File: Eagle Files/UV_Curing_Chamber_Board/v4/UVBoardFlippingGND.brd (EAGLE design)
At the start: 143.3 x 88.4 mm, 29 parts, among them IC1 7805T, IC2 L293D, T1 RFP30N06LE, T2 RFP30N06LE

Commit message: Updated V4
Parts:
- C1, C4, C5, C6, C7: device rcl:C075-063X106 -> rcl:C0603
- C2, C3: device rcl:E1,8-4 -> rcl:C1206
- R1, R2, R3, R5: device rcl:0207/10 -> rcl:R0805
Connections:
- net +5V: now also C3.1; no longer C3.+
- net GND: now also C2.2, C3.2; no longer C2.-, C3.-
- net V+: now also C2.1; no longer C2.+
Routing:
- net +3V3: track 117.3 -> 0.00 mm
- net N$11: track 50.8 -> 0.00 mm
- net N$10: track 48.7 -> 0.00 mm
- net N$25: track 48.0 -> 0.00 mm
- net N$24: track 48.0 -> 0.00 mm
- net N$22: track 46.9 -> 0.00 mm
- net GND: track 17.0 -> 0.00 mm
- net N$17: track 10.4 -> 0.00 mm
- removed copper zone on layer 1, net GND
- removed copper zone on layer 16, net GND
- removed copper zone on layer 1, net V+

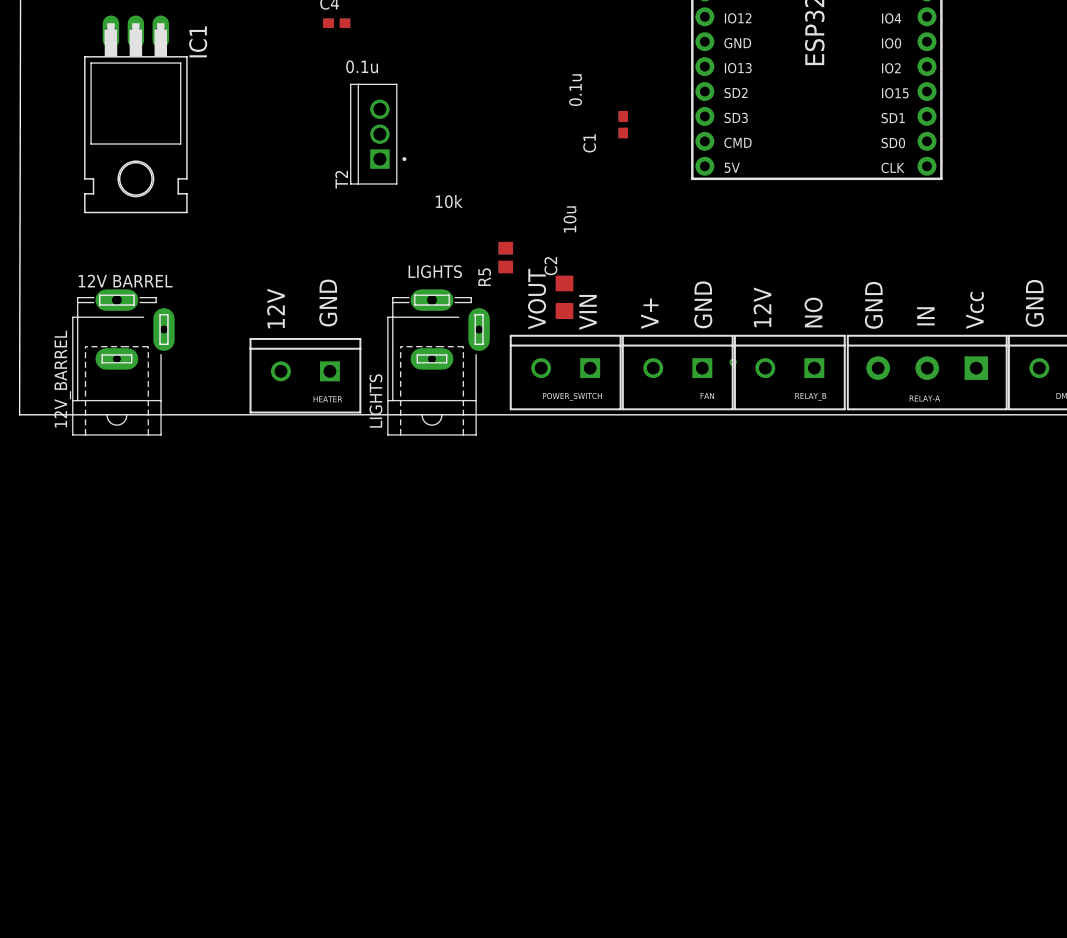
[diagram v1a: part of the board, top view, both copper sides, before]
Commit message: V4 board now has relay circuit on board.
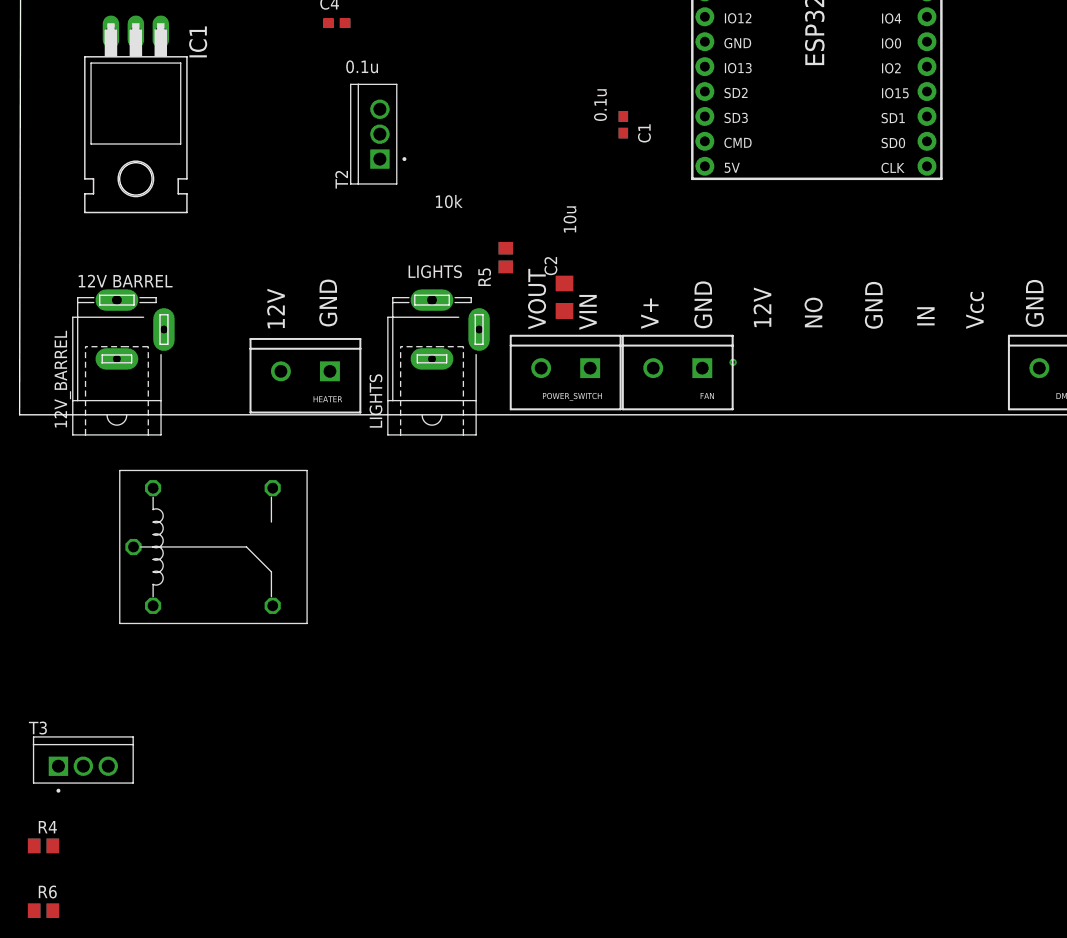
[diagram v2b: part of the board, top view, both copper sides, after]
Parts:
- removed RELAY-A: (no value), SparkFun-Connectors:SCREWTERMINAL-5MM-3
- removed RELAY_B: (no value), SparkFun-Connectors:SCREWTERMINAL-5MM-2
- added R4: 10k, rcl:R0805
- added R6: 220, rcl:R0805
- added T3: RFP30N06LE, RFP30N06LE:TRANS_RFP30N06LE
- added U$2: RELAY, RELAY:RELAY
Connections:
- new net N$31: T3.2, U$2.P$2
- new net N$32: R6.2, U$2.P$1
- net +3V3: no longer DM_SWITCH.1
- net +5V: now also DM_SWITCH.1
- net GND: now also R4.1, T3.3; no longer RELAY-A.3
- net N$16: now also R4.2, T3.1; no longer RELAY-A.2
- net N$28: now also U$2.COM_CPEN; no longer RELAY_B.1
- net N$8: now also R6.1; no longer RELAY-A.1
- net V+: now also U$2.COM; no longer RELAY_B.2

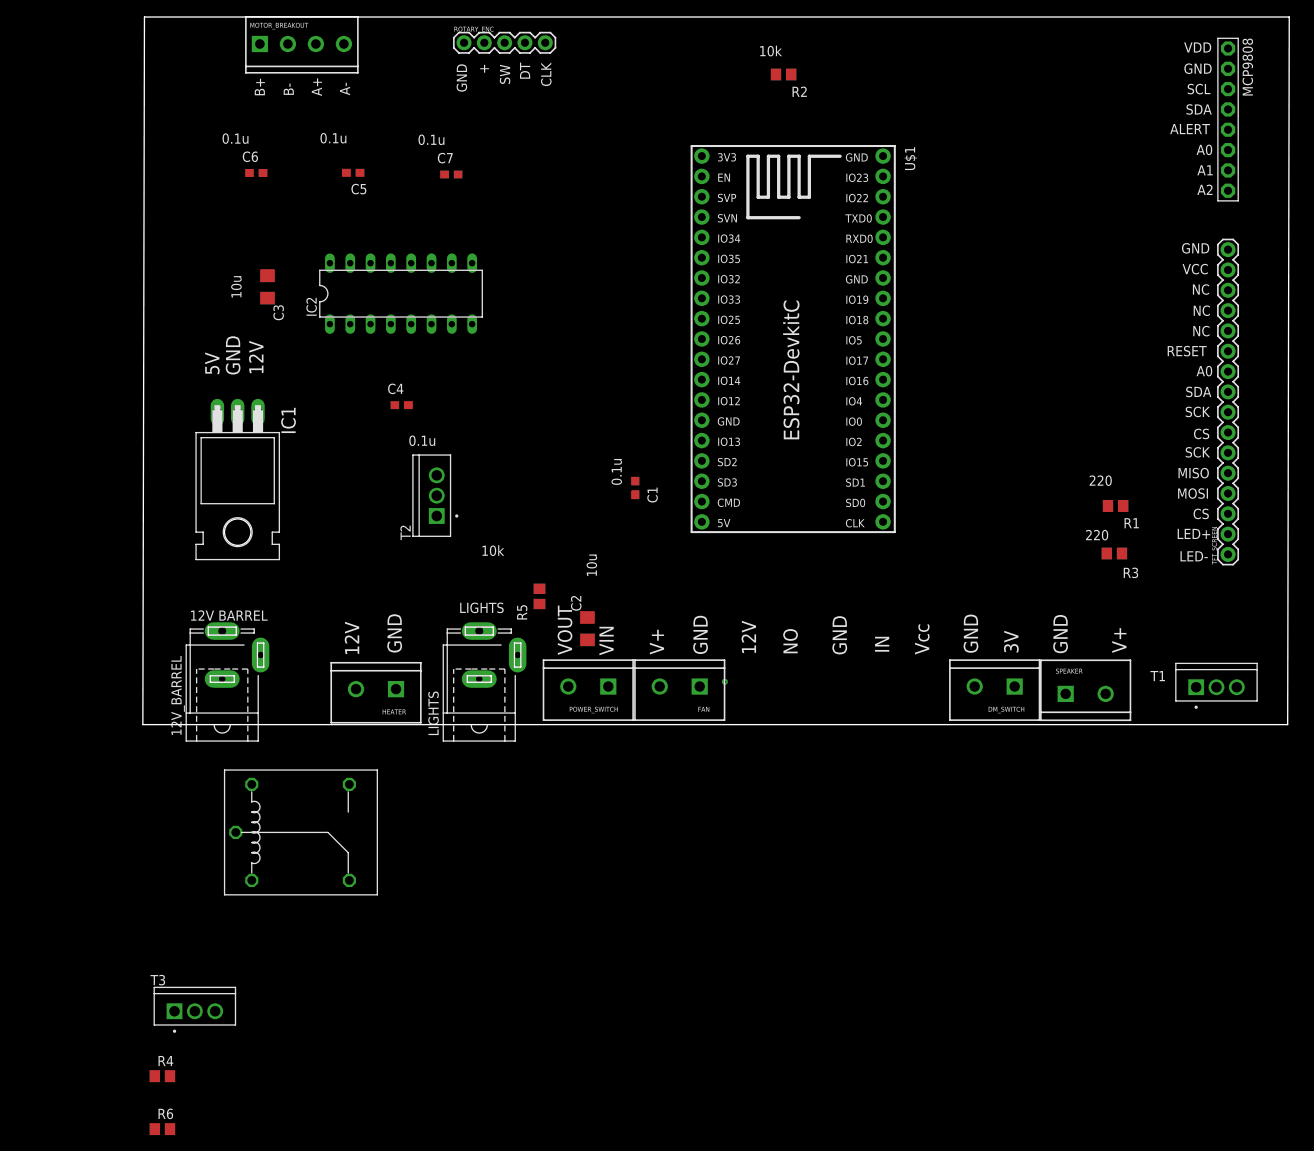
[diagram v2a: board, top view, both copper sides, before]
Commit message: SMD revisions for the PCB
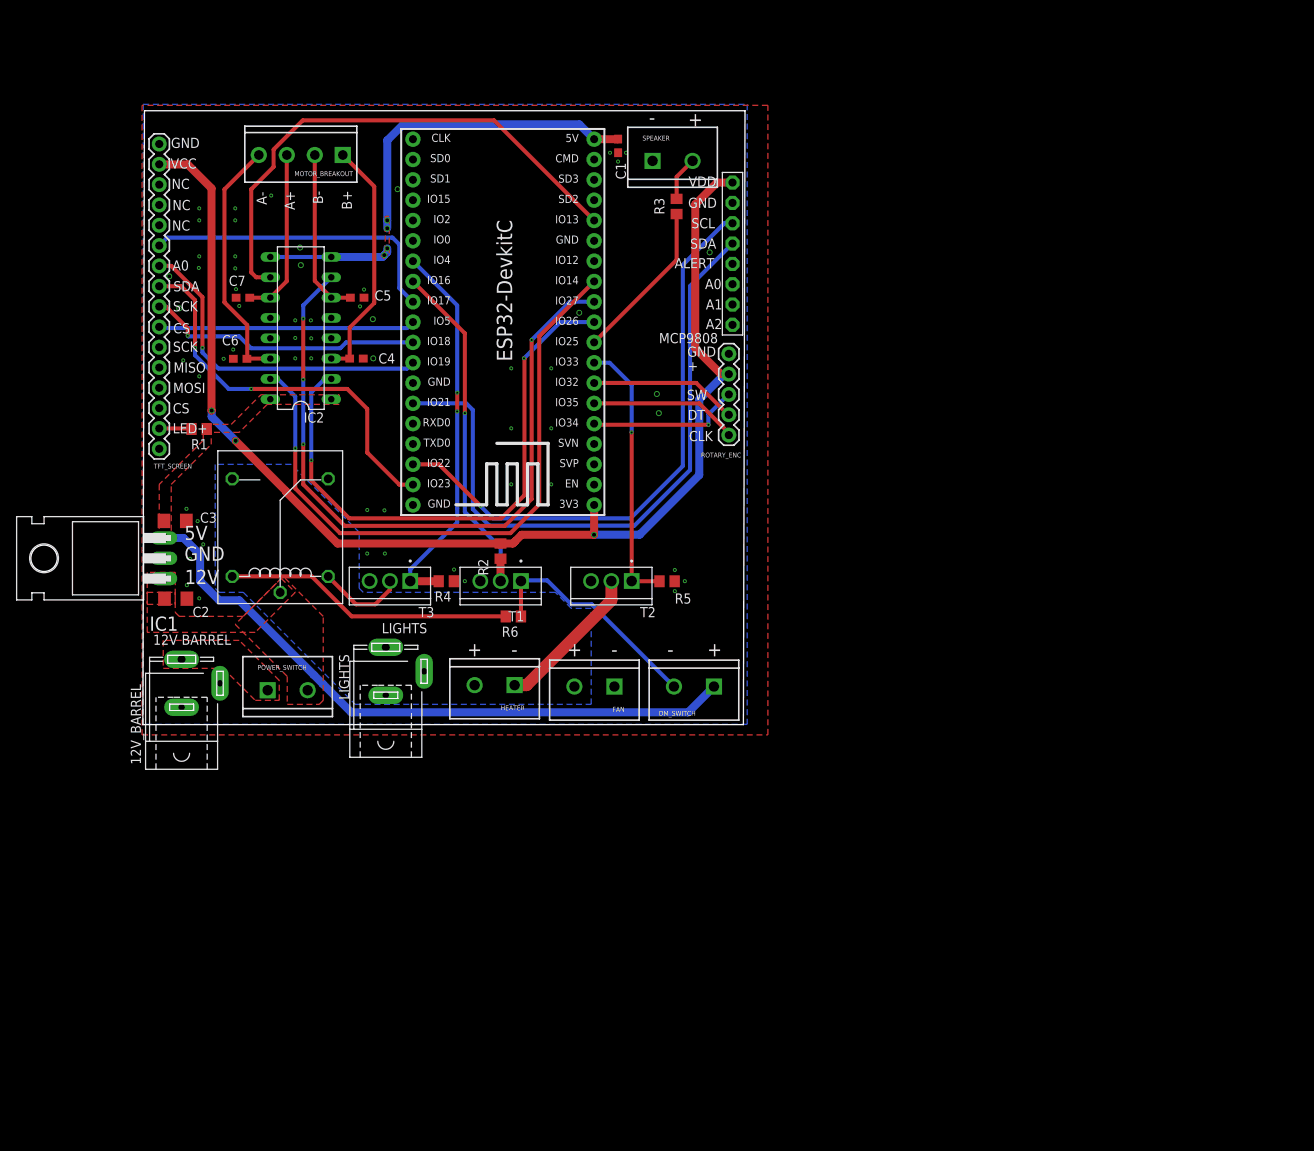
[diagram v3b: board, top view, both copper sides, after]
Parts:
- moved TFT_SCREEN 134.3 mm to (-71.0, -16.1)
- moved R1 115.0 mm to (-66.0, -13.6), turned to 0 degrees
- moved T1 90.5 mm to (-28.3, -32.6), turned to 180 degrees
- moved SPEAKER 84.3 mm to (-9.34, 19.9)
- moved R6 77.7 mm to (-26.7, -37.0), turned to 180 degrees
- moved R4 71.3 mm to (-35.1, -32.6), turned to 180 degrees
- moved R3 69.8 mm to (-6.33, 14.2), turned to 90 degrees
- moved R2 69.3 mm to (-28.3, -28.8), turned to 90 degrees
- moved MCP9808 64.2 mm to (0.66, 8.33)
- moved T3 59.0 mm to (-42.2, -32.6), turned to 180 degrees
- moved C2 51.6 mm to (-68.9, -34.8), turned to 0 degrees
- moved ROTARY_ENC 51.1 mm to (0.20, -4.18), turned to 270 degrees
- moved C1 42.8 mm to (-13.6, 21.8), turned to 270 degrees
- moved POWER_SWITCH 42.6 mm to (-57.4, -46.2), turned to 0 degrees
- moved DM_SWITCH 37.6 mm to (-1.66, -45.8)
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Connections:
- net V+ renamed ASDSFA
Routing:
- net +3V3: track 0.00 -> 155.1 mm, vias 0 -> 3
- net +5V: track 0.00 -> 137.9 mm, vias 0 -> 4
- net N$5: track 0.00 -> 89.1 mm, vias 0 -> 4
- net N$11: track 0.00 -> 81.6 mm
- net N$2: track 0.00 -> 80.5 mm, vias 0 -> 1
- net N$10: track 0.00 -> 72.8 mm, vias 0 -> 1
- net N$13: track 0.00 -> 71.8 mm, vias 0 -> 2
- net N$29: track 0.00 -> 65.9 mm
- net N$1: track 0.00 -> 49.2 mm, vias 0 -> 2
- net N$16: track 0.00 -> 48.3 mm, vias 0 -> 2
- net N$9: track 0.00 -> 44.8 mm, vias 0 -> 1
- net N$22: track 0.00 -> 41.4 mm, vias 0 -> 1
- net N$21: track 0.00 -> 38.6 mm
- net N$32: track 0.00 -> 36.3 mm
- net N$24: track 0.00 -> 34.7 mm, vias 0 -> 1
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- added copper zone on layer 1, net +5V
- added copper zone on layer 1, net ASDSFA
- added copper zone on layer 1, net GND
- added copper zone on layer 16, net GND
- added copper zone on layer 16, net N$28
- added copper zone on layer 1, net N$3
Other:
- board size 143.3 x 88.4 mm -> 75.3 x 76.7 mm
- board text added: "-"
- board text removed: "0.1u"
- board text removed: "10k"
- board text removed: "10u"
- board text removed: "220"
- board text removed: "3V"
- board text removed: "IN"
- board text removed: "LED-"
- board text removed: "NO"
- board text removed: "RESET"
- board text removed: "V+"
- board text removed: "VIN"
- board text removed: "VOUT"
- board text removed: "Vcc"
